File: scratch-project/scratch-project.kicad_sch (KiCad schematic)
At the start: 12 parts, among them J1 Conn_01x10_Pin, J2 Conn_01x10_Pin, J3 Conn_02x10_Top_Bottom, J4 Conn_02x10_Top_Bottom, J5 Conn_02x10_Top_Bottom, J6 Conn_01x10_Pin

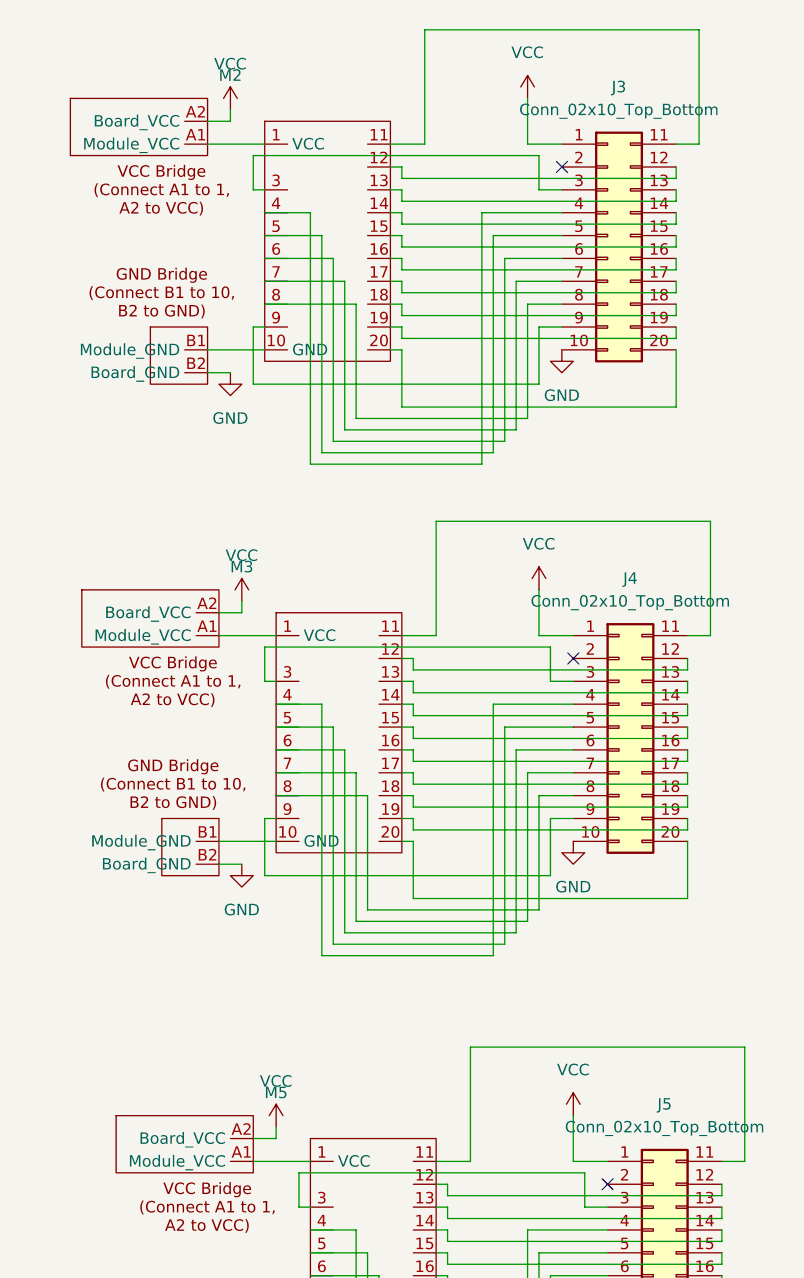
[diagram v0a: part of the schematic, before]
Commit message: fix pad sizes and schematic errors
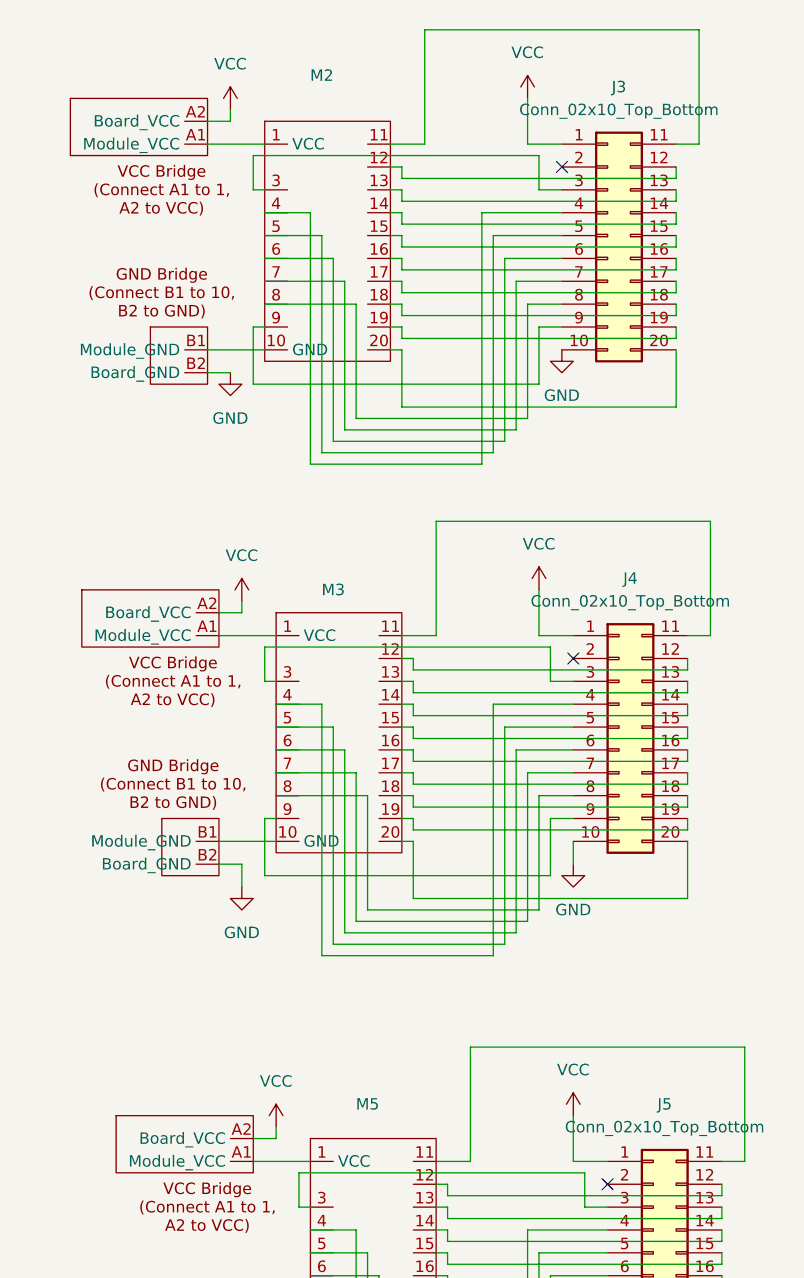
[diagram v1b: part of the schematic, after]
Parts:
- M3: footprint MegaCastle:MegaCastle2x10Wide -> MegaCastle:MegaCastle2x10
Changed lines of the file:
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@@
   (no_connect (at 158.75 149.86))
   (no_connect (at 76.2 29.21))
+  (wire (pts (xy 118.11 114.3) (xy 118.11 116.84))
+    (stroke (width 0) (type default))
+  )
   (wire (pts (xy 119.38 60.96) (xy 151.13 60.96))
     (stroke (width 0) (type default))
@@
     (stroke (width 0) (type default))
   )
+  (wire (pts (xy 154.94 111.76) (xy 154.94 114.3))
+    (stroke (width 0) (type default))
+  )
   (wire (pts (xy 151.13 88.9) (xy 154.94 88.9))
     (stroke (width 0) (type default))
@@
     (stroke (width 0) (type default))
   )
+  (wire (pts (xy 134.62 49.53) (xy 135.89 49.53))
+    (stroke (width 0) (type default))
+  )
+  (wire (pts (xy 119.38 54.61) (xy 119.38 60.96))
+    (stroke (width 0) (type default))
+  )
+  (wire (pts (xy 167.64 101.6) (xy 167.64 102.87))
+    (stroke (width 0) (type default))
+  )
+  (wire (pts (xy 149.86 34.29) (xy 153.67 34.29))
+    (stroke (width 0) (type default))
+  )
+  (wire (pts (xy 137.16 118.11) (xy 137.16 111.76))
+    (stroke (width 0) (type default))
+  )
+  (wire (pts (xy 153.67 41.91) (xy 144.78 41.91))
+    (stroke (width 0) (type default))
+  )
+  (wire (pts (xy 152.4 109.22) (xy 154.94 109.22))
+    (stroke (width 0) (type default))
+  )
+  (wire (pts (xy 76.2 135.89) (xy 83.82 135.89))
+    (stroke (width 0) (type default))
+  )
+  (wire (pts (xy 57.15 93.98) (xy 53.34 93.98))
+    (stroke (width 0) (type default))
+  )
+  (wire (pts (xy 140.97 149.86) (xy 139.7 149.86))
+    (stroke (width 0) (type default))
+  )
+  (wire (pts (xy 171.45 160.02) (xy 171.45 161.29))
+    (stroke (width 0) (type default))
+  )
+  (wire (pts (xy 166.37 41.91) (xy 166.37 43.18))
+    (stroke (width 0) (type default))
+  )
+  (wire (pts (xy 151.13 35.56) (xy 119.38 35.56))
+    (stroke (width 0) (type default))
+  )
+  (wire (pts (xy 53.34 101.6) (xy 83.82 101.6))
+    (stroke (width 0) (type default))
+  )
+  (wire (pts (xy 137.16 100.33) (xy 167.64 100.33))
+    (stroke (width 0) (type default))
+  )
+  (wire (pts (xy 50.8 86.36) (xy 52.07 86.36))
+    (stroke (width 0) (type default))
+  )
+  (wire (pts (xy 124.46 173.99) (xy 156.21 173.99))
+    (stroke (width 0) (type default))
+  )
+  (wire (pts (xy 151.13 157.48) (xy 158.75 157.48))
+    (stroke (width 0) (type default))
+  )
+  (wire (pts (xy 139.7 160.02) (xy 140.97 160.02))
+    (stroke (width 0) (type default))
+  )
+  (wire (pts (xy 135.89 54.61) (xy 135.89 55.88))
+    (stroke (width 0) (type default))
+  )
+  (wire (pts (xy 167.64 96.52) (xy 167.64 97.79))
+    (stroke (width 0) (type default))
+  )
+  (wire (pts (xy 167.64 97.79) (xy 137.16 97.79))
+    (stroke (width 0) (type default))
+  )
+  (wire (pts (xy 144.78 41.91) (xy 144.78 69.85))
+    (stroke (width 0) (type default))
+  )
   (wire (pts (xy 115.57 114.3) (xy 118.11 114.3))
     (stroke (width 0) (type default))
   )
-  (wire (pts (xy 134.62 49.53) (xy 135.89 49.53))
-    (stroke (width 0) (type default))
-  )
-  (wire (pts (xy 119.38 54.61) (xy 119.38 60.96))
-    (stroke (width 0) (type default))
-  )
-  (wire (pts (xy 167.64 101.6) (xy 167.64 102.87))
-    (stroke (width 0) (type default))
-  )
-  (wire (pts (xy 149.86 34.29) (xy 153.67 34.29))
-    (stroke (width 0) (type default))
-  )
-  (wire (pts (xy 137.16 118.11) (xy 137.16 111.76))
-    (stroke (width 0) (type default))
-  )
-  (wire (pts (xy 153.67 41.91) (xy 144.78 41.91))
-    (stroke (width 0) (type default))
-  )
-  (wire (pts (xy 152.4 109.22) (xy 154.94 109.22))
-    (stroke (width 0) (type default))
-  )
-  (wire (pts (xy 76.2 135.89) (xy 83.82 135.89))
-    (stroke (width 0) (type default))
-  )
-  (wire (pts (xy 57.15 93.98) (xy 53.34 93.98))
-    (stroke (width 0) (type default))
-  )
-  (wire (pts (xy 140.97 149.86) (xy 139.7 149.86))
-    (stroke (width 0) (type default))
-  )
-  (wire (pts (xy 171.45 160.02) (xy 171.45 161.29))
-    (stroke (width 0) (type default))
-  )
-  (wire (pts (xy 166.37 41.91) (xy 166.37 43.18))
-    (stroke (width 0) (type default))
-  )
-  (wire (pts (xy 151.13 35.56) (xy 119.38 35.56))
-    (stroke (width 0) (type default))
-  )
-  (wire (pts (xy 53.34 101.6) (xy 83.82 101.6))
-    (stroke (width 0) (type default))
-  )
-  (wire (pts (xy 137.16 100.33) (xy 167.64 100.33))
-    (stroke (width 0) (type default))
-  )
-  (wire (pts (xy 50.8 86.36) (xy 52.07 86.36))
-    (stroke (width 0) (type default))
-  )
-  (wire (pts (xy 124.46 173.99) (xy 156.21 173.99))
-    (stroke (width 0) (type default))
-  )
-  (wire (pts (xy 151.13 157.48) (xy 158.75 157.48))
-    (stroke (width 0) (type default))
-  )
-  (wire (pts (xy 139.7 160.02) (xy 140.97 160.02))
-    (stroke (width 0) (type default))
-  )
-  (wire (pts (xy 135.89 54.61) (xy 135.89 55.88))
-    (stroke (width 0) (type default))
-  )
-  (wire (pts (xy 167.64 96.52) (xy 167.64 97.79))
-    (stroke (width 0) (type default))
-  )
-  (wire (pts (xy 167.64 97.79) (xy 137.16 97.79))
-    (stroke (width 0) (type default))
-  )
-  (wire (pts (xy 144.78 41.91) (xy 144.78 69.85))
-    (stroke (width 0) (type default))
-  )
   (wire (pts (xy 120.65 109.22) (xy 120.65 115.57))
     (stroke (width 0) (type default))
@@
   (wire (pts (xy 135.89 39.37) (xy 135.89 40.64))
     (stroke (width 0) (type default))
-  )
-  (symbol (lib_id "power:GND") (at 154.94 111.76 0) (unit 1)
-    (in_bom yes) (on_board yes) (dnp no) (fields_autoplaced)
-    (property "Reference" "#PWR014" (at 154.94 118.11 0)
-      (effects (font (size 1.27 1.27)) hide)
-    )
-    (property "Value" "GND" (at 154.94 116.84 0)
-      (effects (font (size 1.27 1.27)))
-    )
-    (property "Footprint" "" (at 154.94 111.76 0)
-      (effects (font (size 1.27 1.27)) hide)
-    )
-    (property "Datasheet" "" (at 154.94 111.76 0)
-      (effects (font (size 1.27 1.27)) hide)
-    )
-    (pin "1")
-    (instances
-      (project "scratch-project"
-        (path "/c4fc3aa5-a656-49f5-a50f-7ae2bfded0aa"
-          (reference "#PWR014") (unit 1)
-        )
-      )
-    )
   )
   (symbol (lib_id "power:VCC") (at 154.94 142.24 0) (unit 1)
@@
   )
   (symbol (lib_name "MegaCastle2x10_1") (lib_id "MegaCastle:MegaCastle2x10") (at 132.08 158.75 0) (unit 1)
-    (in_bom yes) (on_board yes) (dnp no) (fields_autoplaced)
-    (property "Reference" "M5" (at 121.92 139.7 0)
+    (in_bom yes) (on_board yes) (dnp no)
+    (property "Reference" "M5" (at 132.08 140.97 0)
       (effects (font (size 1.27 1.27)))
     )
@@
   )
   (symbol (lib_name "MegaCastle2x10_1") (lib_id "MegaCastle:MegaCastle2x10") (at 128.27 100.33 0) (unit 1)
-    (in_bom yes) (on_board yes) (dnp no) (fields_autoplaced)
-    (property "Reference" "M3" (at 118.11 81.28 0)
+    (in_bom yes) (on_board yes) (dnp no)
+    (property "Reference" "M3" (at 128.27 83.82 0)
       (effects (font (size 1.27 1.27)))
     )
@@
       (effects (font (size 1.27 1.27)))
     )
-    (property "Footprint" "MegaCastle:MegaCastle2x10Wide" (at 128.27 95.25 0)
+    (property "Footprint" "MegaCastle:MegaCastle2x10" (at 128.27 95.25 0)
       (effects (font (size 1.27 1.27)) hide)
     )
@@
   )
   (symbol (lib_name "MegaCastle2x10_1") (lib_id "MegaCastle:MegaCastle2x10") (at 127 45.72 0) (unit 1)
-    (in_bom yes) (on_board yes) (dnp no) (fields_autoplaced)
-    (property "Reference" "M2" (at 116.84 26.67 0)
+    (in_bom yes) (on_board yes) (dnp no)
+    (property "Reference" "M2" (at 127 26.67 0)
       (effects (font (size 1.27 1.27)))
     )
@@
     )
   )
+  (symbol (lib_id "power:GND") (at 118.11 116.84 0) (unit 1)
+    (in_bom yes) (on_board yes) (dnp no) (fields_autoplaced)
+    (property "Reference" "#PWR012" (at 118.11 123.19 0)
+      (effects (font (size 1.27 1.27)) hide)
+    )
+    (property "Value" "GND" (at 118.11 121.92 0)
+      (effects (font (size 1.27 1.27)))
+    )
+    (property "Footprint" "" (at 118.11 116.84 0)
+      (effects (font (size 1.27 1.27)) hide)
+    )
+    (property "Datasheet" "" (at 118.11 116.84 0)
+      (effects (font (size 1.27 1.27)) hide)
+    )
+    (pin "1")
+    (instances
+      (project "scratch-project"
+        (path "/c4fc3aa5-a656-49f5-a50f-7ae2bfded0aa"
+          (reference "#PWR012") (unit 1)
+        )
+      )
+    )
+  )
   (symbol (lib_id "power:GND") (at 153.67 57.15 0) (unit 1)
     (in_bom yes) (on_board yes) (dnp no) (fields_autoplaced)
@@
     )
   )
+  (symbol (lib_id "power:GND") (at 154.94 114.3 0) (unit 1)
+    (in_bom yes) (on_board yes) (dnp no) (fields_autoplaced)
+    (property "Reference" "#PWR014" (at 154.94 120.65 0)
+      (effects (font (size 1.27 1.27)) hide)
+    )
+    (property "Value" "GND" (at 154.94 119.38 0)
+      (effects (font (size 1.27 1.27)))
+    )
+    (property "Footprint" "" (at 154.94 114.3 0)
+      (effects (font (size 1.27 1.27)) hide)
+    )
+    (property "Datasheet" "" (at 154.94 114.3 0)
+      (effects (font (size 1.27 1.27)) hide)
+    )
+    (pin "1")
+    (instances
+      (project "scratch-project"
+        (path "/c4fc3aa5-a656-49f5-a50f-7ae2bfded0aa"
+          (reference "#PWR014") (unit 1)
+        )
+      )
+    )
+  )
   (symbol (lib_id "power:VCC") (at 71.12 76.2 0) (unit 1)
     (in_bom yes) (on_board yes) (dnp no) (fields_autoplaced)
@@
         )
       )
-    )
-  )
-  (symbol (lib_id "power:GND") (at 118.11 114.3 0) (unit 1)
-    (in_bom yes) (on_board yes) (dnp no) (fields_autoplaced)
-    (property "Reference" "#PWR012" (at 118.11 120.65 0)
-      (effects (font (size 1.27 1.27)) hide)
-    )
-    (property "Value" "GND" (at 118.11 119.38 0)
-      (effects (font (size 1.27 1.27)))
-    )
-    (property "Footprint" "" (at 118.11 114.3 0)
-      (effects (font (size 1.27 1.27)) hide)
-    )
-    (property "Datasheet" "" (at 118.11 114.3 0)
-      (effects (font (size 1.27 1.27)) hide)
-    )
-    (pin "1")
-    (instances
-      (project "scratch-project"
-        (path "/c4fc3aa5-a656-49f5-a50f-7ae2bfded0aa"
-          (reference "#PWR012") (unit 1)
-        )
-      )

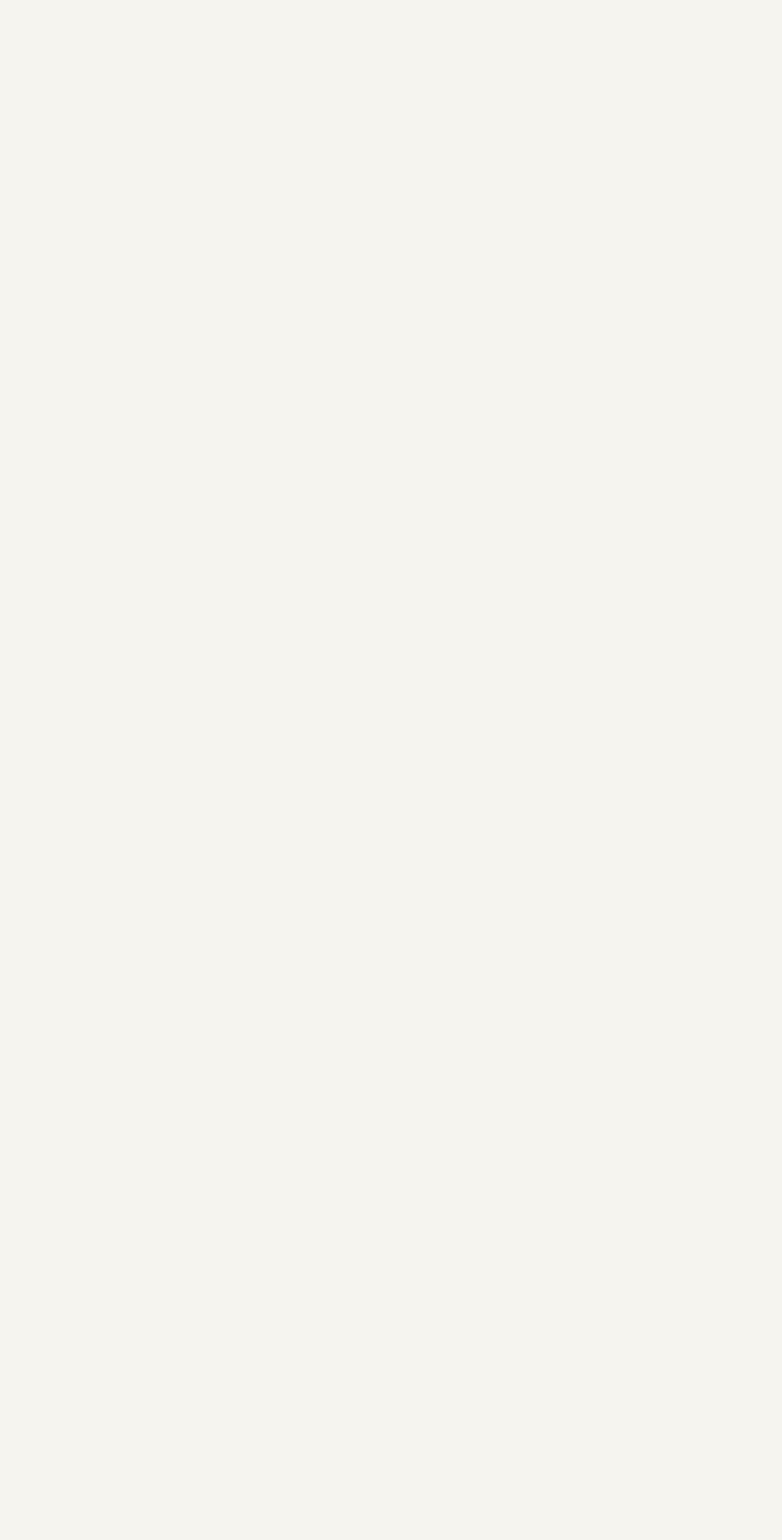
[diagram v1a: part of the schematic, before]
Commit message: fix 2x10 wide footprint. add modules to scratch board
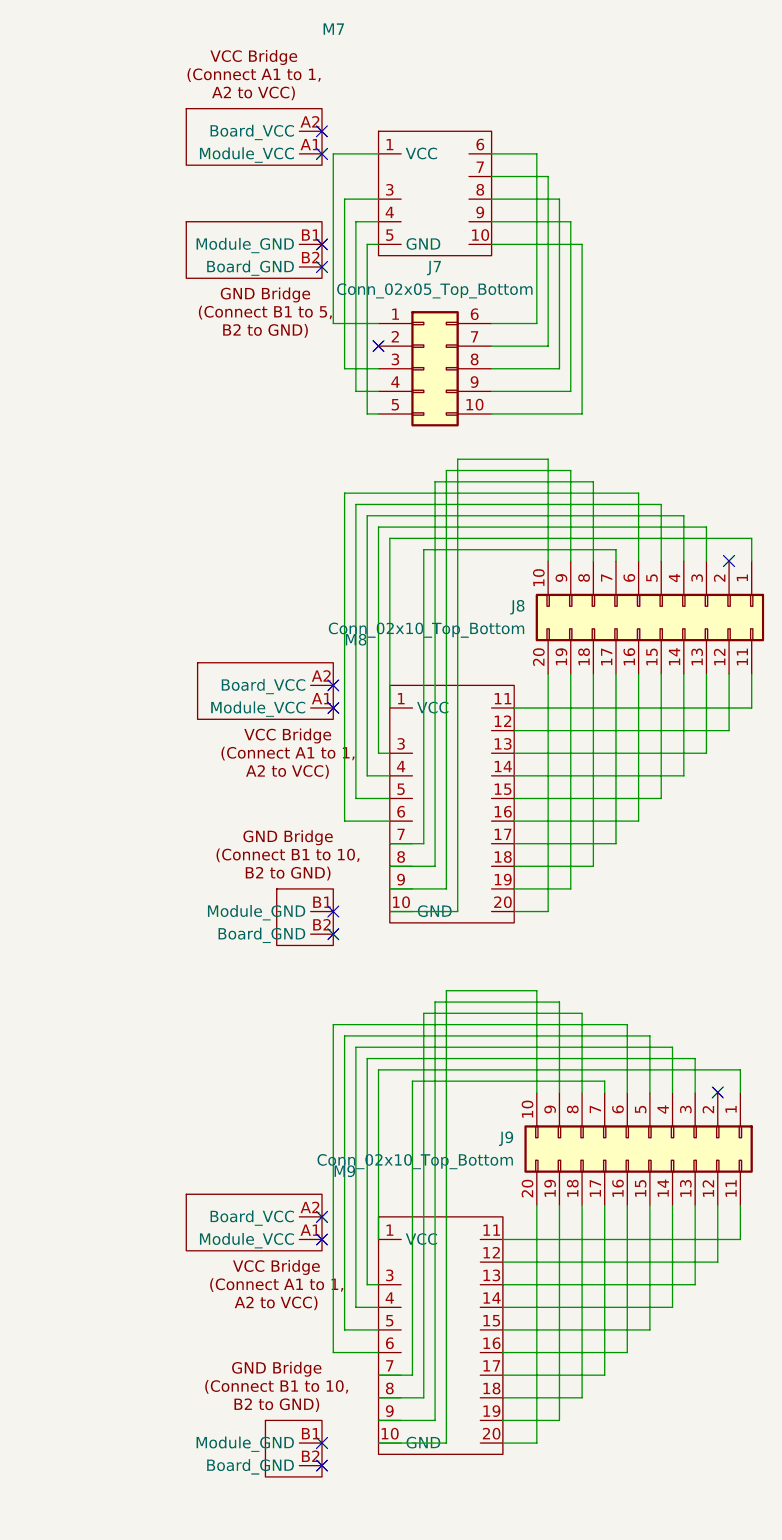
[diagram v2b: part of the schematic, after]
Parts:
- added J7: Conn_02x05_Top_Bottom, Connector_PinHeader_1.27mm:PinHeader_2x05_P1.27mm_Vertical, symbol Connector_Generic:Conn_02x05_Top_Bottom
- added J8, J9: Conn_02x10_Top_Bottom, Connector_PinHeader_1.27mm:PinHeader_2x10_P1.27mm_Vertical, symbol Connector_Generic:Conn_02x10_Top_Bottom
- added M7: ~, MegaCastle:MegaCastle2x5-Module, symbol MegaCastle:MegaCastle2x5
- added M8: ~, MegaCastle:MegaCastle2x10-Module, symbol MegaCastle:MegaCastle2x10
- added M9: ~, MegaCastle:MegaCastle2x10Wide-Module, symbol MegaCastle:MegaCastle2x10
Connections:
- new net: J8.1 (Pin_1), M8.1 (VCC)
- new net: J8.10 (Pin_10), M8.10 (GND)
- new net: J8.11 (Pin_11), M8.11
- new net: J8.12 (Pin_12), M8.12
- new net: J8.13 (Pin_13), M8.13
- new net: J8.14 (Pin_14), M8.14
- new net: J8.15 (Pin_15), M8.15
- new net: J8.16 (Pin_16), M8.16
- new net: J8.17 (Pin_17), M8.17
- new net: J8.18 (Pin_18), M8.18
- new net: J8.19 (Pin_19), M8.19
- new net: J8.20 (Pin_20), M8.20
- new net: J8.3 (Pin_3), M8.3
- new net: J8.4 (Pin_4), M8.4
- new net: J8.5 (Pin_5), M8.5
- new net: J8.6 (Pin_6), M8.6
- new net: J8.7 (Pin_7), M8.7
- new net: J8.8 (Pin_8), M8.8
- new net: J8.9 (Pin_9), M8.9
- new net: J9.1 (Pin_1), M9.1 (VCC)
- new net: J9.10 (Pin_10), M9.10 (GND)
- new net: J9.11 (Pin_11), M9.11
- new net: J9.12 (Pin_12), M9.12
- new net: J9.13 (Pin_13), M9.13
- new net: J9.14 (Pin_14), M9.14
- new net: J9.15 (Pin_15), M9.15
- new net: J9.16 (Pin_16), M9.16
- new net: J9.17 (Pin_17), M9.17
- new net: J9.18 (Pin_18), M9.18
- new net: J9.19 (Pin_19), M9.19
- new net: J9.20 (Pin_20), M9.20
- new net: J9.3 (Pin_3), M9.3
- new net: J9.4 (Pin_4), M9.4
- new net: J9.5 (Pin_5), M9.5
- new net: J9.6 (Pin_6), M9.6
- new net: J9.7 (Pin_7), M9.7
- new net: J9.8 (Pin_8), M9.8
- new net: J9.9 (Pin_9), M9.9
- new net: J7.1 (Pin_1), M7.1 (VCC)
- new net: J7.10 (Pin_10), M7.10
- new net: J7.3 (Pin_3), M7.3
- new net: J7.4 (Pin_4), M7.4
- new net: J7.5 (Pin_5), M7.5 (GND)
- new net: J7.6 (Pin_6), M7.6
- new net: J7.7 (Pin_7), M7.7
- new net: J7.8 (Pin_8), M7.8
- new net: J7.9 (Pin_9), M7.9
- no-connect marks 4 -> 19
